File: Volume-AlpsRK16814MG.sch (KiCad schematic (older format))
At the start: 9 parts, among them P1 AB I/O, P2 CD I/O, P3 VD, P4 CTRL, P5 GND, U1 SN754410

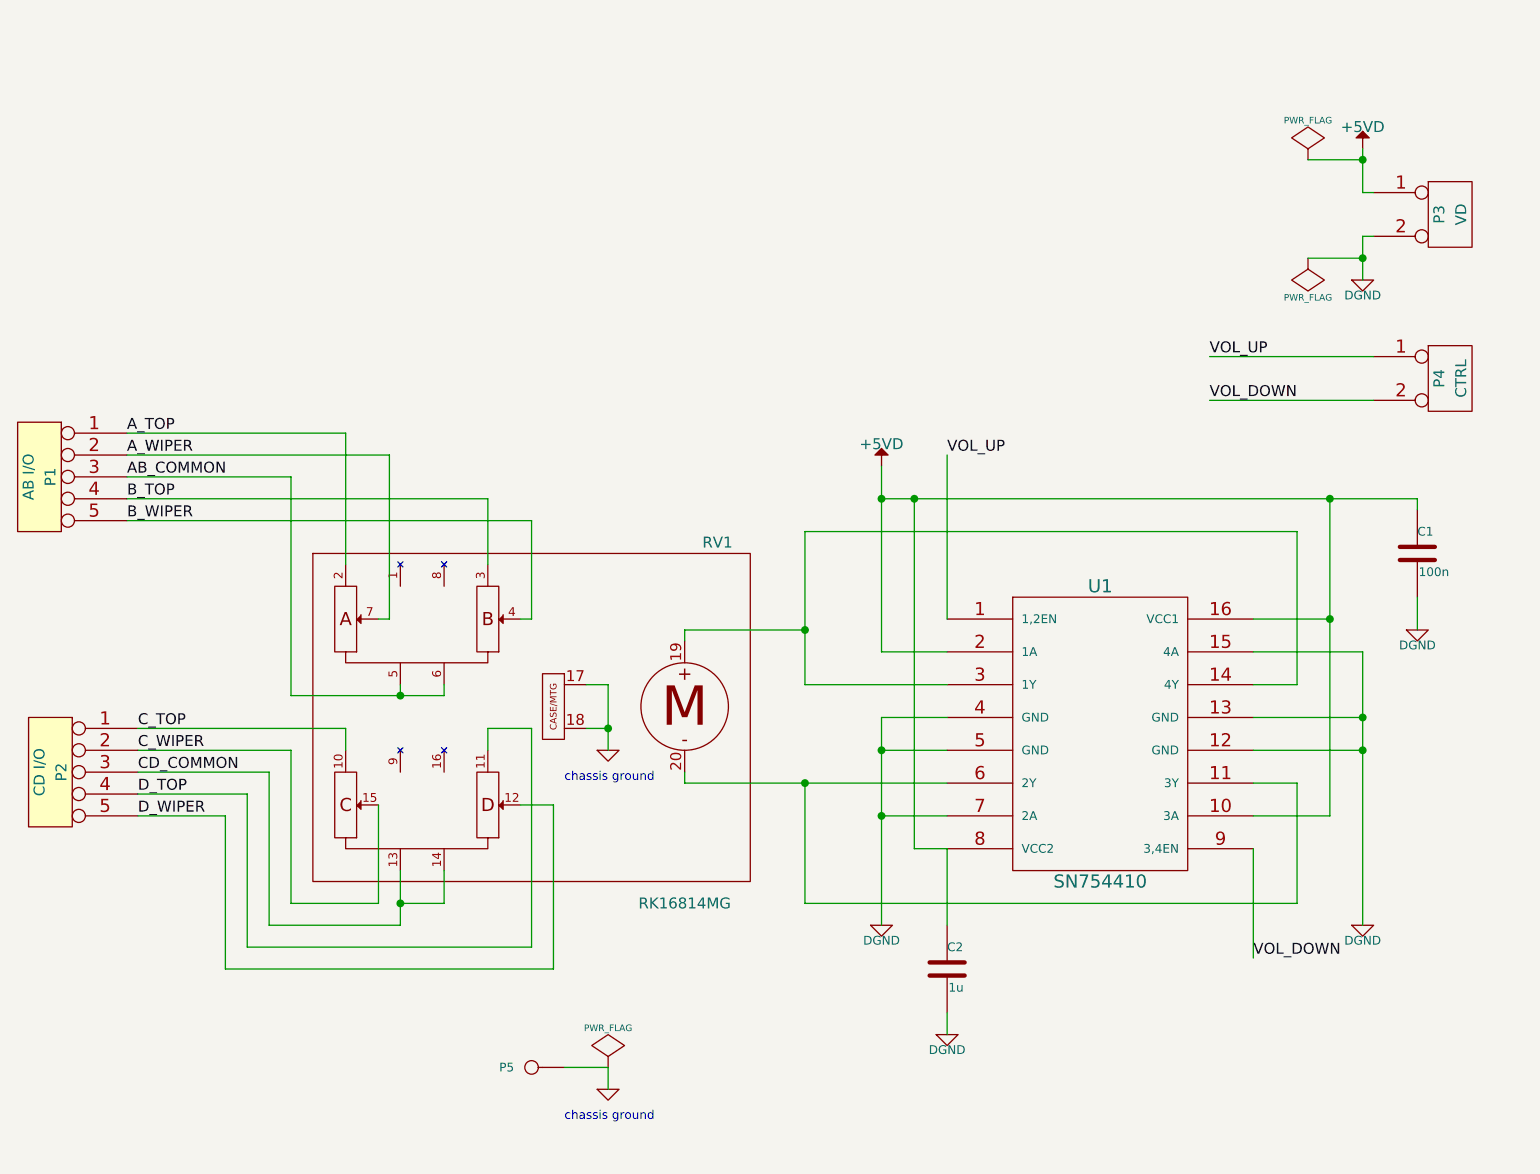
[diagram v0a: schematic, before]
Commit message: Silkscreen optimizations. Added license to silkscreen.
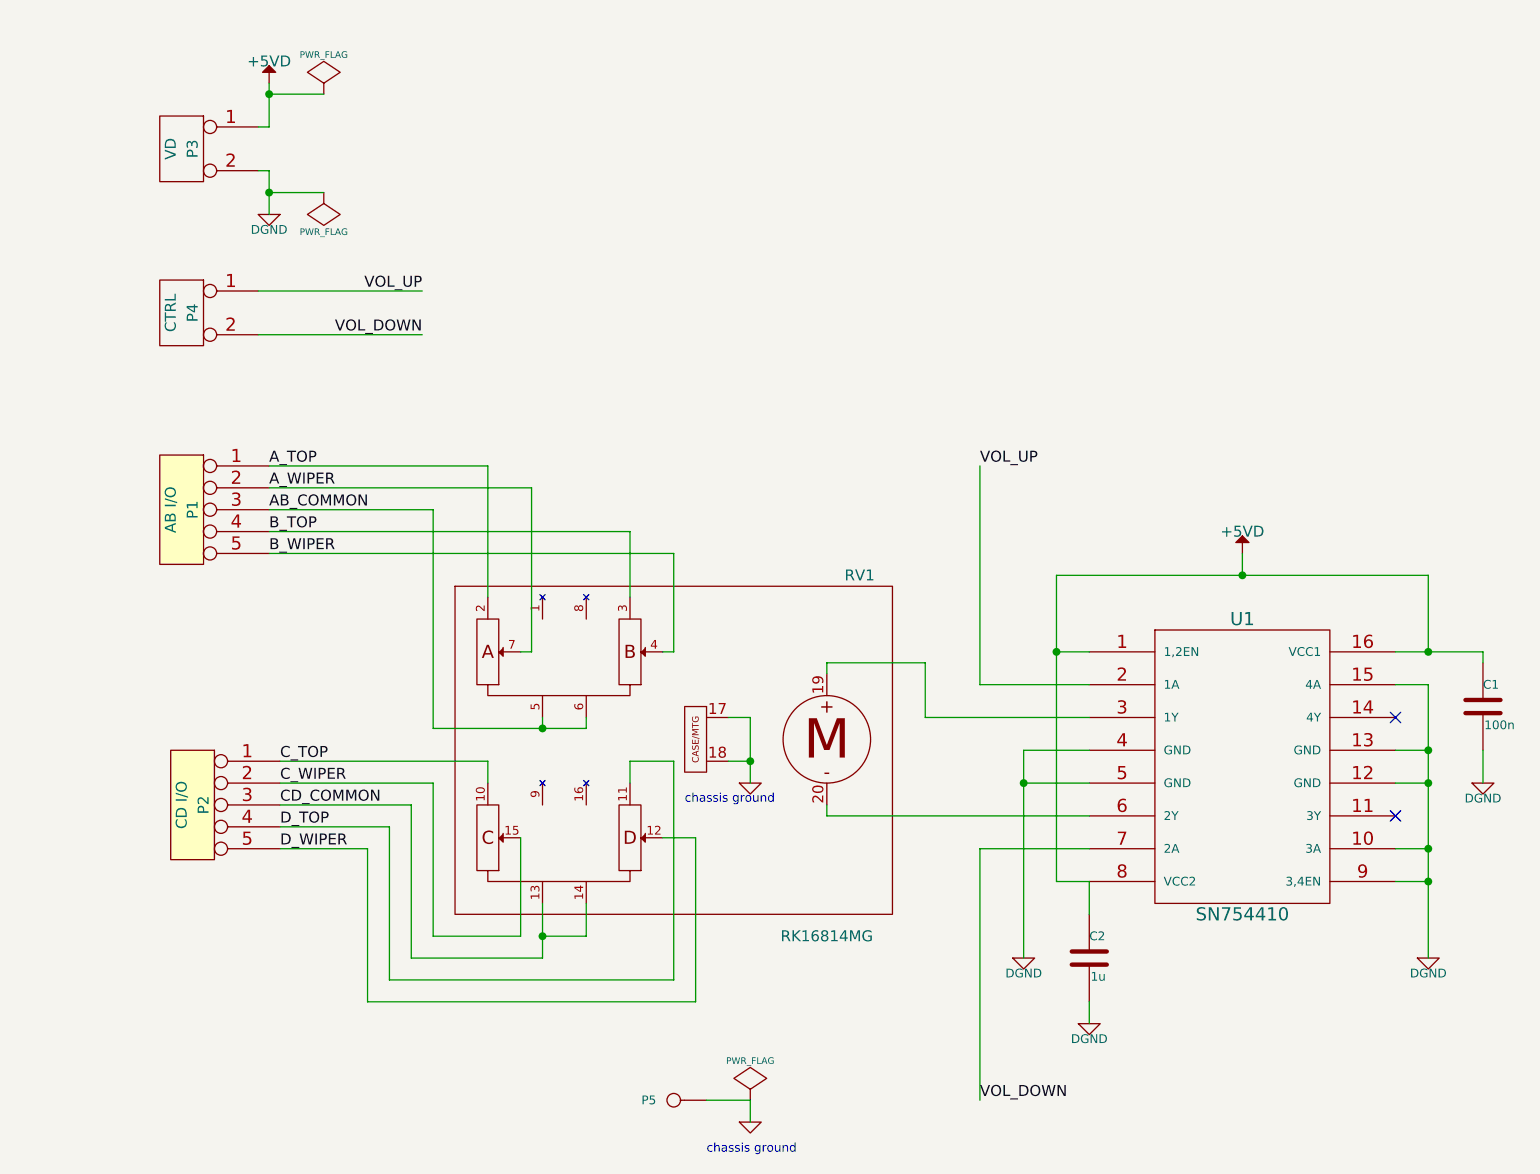
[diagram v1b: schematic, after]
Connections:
- net +5VD: now also U1.1 (1,2EN); no longer U1.10 (3A), U1.2 (1A)
- net DGND: now also U1.10 (3A), U1.9 (3,4EN); no longer U1.7 (2A)
- net VOL_DOWN: now also U1.7 (2A); no longer U1.9 (3,4EN)
- net VOL_UP: now also U1.2 (1A); no longer U1.1 (1,2EN)
- net at RV1.20 (Vmotor-), U1.6 (2Y): no longer U1.11 (3Y)
- net at RV1.19 (Vmotor+), U1.3 (1Y): no longer U1.14 (4Y)
- no-connect marks 0 -> 2
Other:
- moved on the sheet: C1, C2, P1, P2, P3, P4, P5, RV1, U1

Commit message: Schematic changes for independent motor drive voltage.
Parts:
- removed P3: VD, mfk-TE_282834-2, symbol CONN_2
- added P3: V, symbol CONN_3
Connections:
- net +5VD: now also P3.2 (PM); no longer C2.1, U1.8 (VCC2)
- net DGND: now also P3.3 (P3)
- new net V_MOTOR: C2.1, P3.1 (P1), U1.8 (VCC2)
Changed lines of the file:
@@
 Sheet 1 1
 Title "ALPS RK16816MG with H-bridge"
-Date "24 mar 2015"
+Date "3 apr 2015"
 Rev ""
 Comp "Mithat Konar"
@@
 L DGND #PWR02
 U 1 1 550CA86E
-P 6600 5500
-F 0 "#PWR02" H 6600 5500 40  0001 C CNN
-F 1 "DGND" H 6600 5430 40  0000 C CNN
-F 2 "" H 6600 5500 60  0000 C CNN
-F 3 "" H 6600 5500 60  0000 C CNN
-	1    6600 5500
+P 6600 5300
+F 0 "#PWR02" H 6600 5300 40  0001 C CNN
+F 1 "DGND" H 6600 5230 40  0000 C CNN
+F 2 "" H 6600 5300 60  0000 C CNN
+F 3 "" H 6600 5300 60  0000 C CNN
+	1    6600 5300
 	1    0    0    -1
 $EndComp
@@
 	6900 4550 6600 4550
 Wire Wire Line
-	6600 4550 6600 5500
+	6600 4550 6600 5300
 Wire Wire Line
 	6900 4700 6600 4700
@@
 Wire Wire Line
 	6750 5150 6900 5150
-Wire Wire Line
-	6750 3750 6750 5150
 $Comp
 L C C1
@@
 Wire Wire Line
 	8700 4700 8700 4550
-Text Label 6400 3250 0    50   ~ 0
+Text Label 6400 3250 3    50   ~ 0
 VOL_UP
-Text Label 6400 6150 0    50   ~ 0
+Text Label 6400 6150 1    50   ~ 0
 VOL_DOWN
 $Comp
@@
 $EndComp
 Wire Wire Line
-	3150 1700 3100 1700
-Wire Wire Line
-	3150 1500 3150 1700
+	3650 1350 3650 1800
 Wire Wire Line
 	3100 2450 3850 2450
@@
 L PWR_FLAG #FLG06
 U 1 1 550CB3CC
-P 3400 1550
-F 0 "#FLG06" H 3400 1645 30  0001 C CNN
-F 1 "PWR_FLAG" H 3400 1730 30  0000 C CNN
-F 2 "" H 3400 1550 60  0000 C CNN
-F 3 "" H 3400 1550 60  0000 C CNN
-	1    3400 1550
+P 3900 1650
+F 0 "#FLG06" H 3900 1745 30  0001 C CNN
+F 1 "PWR_FLAG" H 3900 1830 30  0000 C CNN
+F 2 "" H 3900 1650 60  0000 C CNN
+F 3 "" H 3900 1650 60  0000 C CNN
+	1    3900 1650
 	-1   0    0    -1
 $EndComp
@@
 	3150 1900 3150 2100
 Wire Wire Line
-	3400 1550 3150 1550
-Connection ~ 3150 1550
+	3900 1650 3650 1650
+Connection ~ 3650 1650
 Wire Wire Line
 	3400 2000 3150 2000
 Connection ~ 3150 2000
-$Comp
-L CONN_2 P3
-U 1 1 550CCC99
-P 2750 1800
-F 0 "P3" V 2700 1800 50  0000 C CNN
-F 1 "VD" V 2800 1800 50  0000 C CNN
-F 2 "mfk-TE_282834-2" H 2750 1800 60  0001 C CNN
-F 3 "" H 2750 1800 60  0000 C CNN
-	1    2750 1800
-	-1   0    0    -1
-$EndComp
 $Comp
 L CONN_2 P4
@@
 L +5VD #PWR08
 U 1 1 550CE733
-P 3150 1500
-F 0 "#PWR08" H 3150 1450 20  0001 C CNN
-F 1 "+5VD" H 3150 1600 50  0000 C CNN
-F 2 "" H 3150 1500 60  0000 C CNN
-F 3 "" H 3150 1500 60  0000 C CNN
-	1    3150 1500
+P 3650 1350
+F 0 "#PWR08" H 3650 1300 20  0001 C CNN
+F 1 "+5VD" H 3650 1450 50  0000 C CNN
+F 2 "" H 3650 1350 60  0000 C CNN
+F 3 "" H 3650 1350 60  0000 C CNN
+	1    3650 1350
 	-1   0    0    -1
 $EndComp
@@
 63 98 05 E1 6B C4 72 91 8E EA 95 27 8C 4B 0B 6B 30 6B 95 2D 08 DF 47 79 14 D8 40 20 A9 90 96 2D
 E1 E7 3D C6 74 F3 E0 6E B9 00 E4 0E CC EC 2A 00 9E 03 F9 2E 43 53 93 3B E7 B1 3D FE 0F E4 2C B5
-B8 3A B8 3B 5D 00 00 00 00 49 45 4E 44 AE 42 60 82 30 $EndBitmap
+B8 3A B8 3B 5D 00 00 00 00 49 45 4E 44 AE 42 60 82 69 $EndBitmap
 EndData
 $EndBitmap
@@
 Wire Wire Line
 	6900 4100 6750 4100
-Connection ~ 6750 4100
 Wire Wire Line
 	6150 4150 6150 4400
@@
 Wire Wire Line
 	6400 5000 6400 6150
+$Comp
+L CONN_3 P3
+U 1 1 551F2247
+P 2750 1800
+F 0 "P3" V 2700 1800 50  0000 C CNN
+F 1 "V" V 2800 1800 40  0000 C CNN
+F 2 "" H 2750 1800 60  0000 C CNN
+F 3 "" H 2750 1800 60  0000 C CNN
+	1    2750 1800
+	-1   0    0    -1
+$EndComp
+Wire Wire Line
+	3650 1800 3100 1800
+Wire Wire Line
+	3100 1700 3350 1700
+Wire Wire Line
+	3150 1250 3150 1700
+Text Label 3150 1250 3    60   ~ 0
+V_MOTOR
+Wire Wire Line
+	6750 4100 6750 3750
+Wire Wire Line
+	6750 5150 6750 6150
+Text Label 6750 6150 1    60   ~ 0
+V_MOTOR
+$Comp
+L PWR_FLAG #FLG013
+U 1 1 551F243F
+P 3350 1650
+F 0 "#FLG013" H 3350 1745 30  0001 C CNN
+F 1 "PWR_FLAG" H 3350 1830 30  0000 C CNN
+F 2 "" H 3350 1650 60  0000 C CNN
+F 3 "" H 3350 1650 60  0000 C CNN
+	1    3350 1650
+	-1   0    0    -1
+$EndComp
+Connection ~ 3150 1700
+Wire Wire Line
+	3350 1700 3350 1650
 $EndSCHEMATC

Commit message: Added jumper to connect motor and digital supplies to schematic; PCB updated.
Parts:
- added J1: PWR_BR, mfk-SIL-2, symbol JUMPER
- P3: value V -> PWR; footprint (none) -> mfk-TE_282834-3
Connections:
- net +5VD: now also J1.1
- net V_MOTOR renamed V_MOT
- net V_MOT: now also J1.2
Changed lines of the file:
@@
 Sheet 1 1
 Title "ALPS RK16816MG with H-bridge"
-Date "3 apr 2015"
+Date "4 apr 2015"
 Rev ""
 Comp "Mithat Konar"
@@
 63 98 05 E1 6B C4 72 91 8E EA 95 27 8C 4B 0B 6B 30 6B 95 2D 08 DF 47 79 14 D8 40 20 A9 90 96 2D
 E1 E7 3D C6 74 F3 E0 6E B9 00 E4 0E CC EC 2A 00 9E 03 F9 2E 43 53 93 3B E7 B1 3D FE 0F E4 2C B5
-B8 3A B8 3B 5D 00 00 00 00 49 45 4E 44 AE 42 60 82 69 $EndBitmap
+B8 3A B8 3B 5D 00 00 00 00 49 45 4E 44 AE 42 60 82 14 $EndBitmap
 EndData
 $EndBitmap
@@
 P 2750 1800
 F 0 "P3" V 2700 1800 50  0000 C CNN
-F 1 "V" V 2800 1800 40  0000 C CNN
-F 2 "" H 2750 1800 60  0000 C CNN
+F 1 "PWR" V 2800 1800 40  0000 C CNN
+F 2 "mfk-TE_282834-3" H 2750 1800 60  0001 C CNN
 F 3 "" H 2750 1800 60  0000 C CNN
 	1    2750 1800
@@
 	3150 1250 3150 1700
 Text Label 3150 1250 3    60   ~ 0
-V_MOTOR
+V_MOT
 Wire Wire Line
 	6750 4100 6750 3750
@@
 	6750 5150 6750 6150
 Text Label 6750 6150 1    60   ~ 0
-V_MOTOR
+V_MOT
 $Comp
 L PWR_FLAG #FLG013
@@
 Wire Wire Line
 	3350 1700 3350 1650
+$Comp
+L JUMPER J1
+U 1 1 552023B1
+P 4750 1800
+F 0 "J1" H 4750 1950 60  0000 C CNN
+F 1 "PWR_BR" H 4750 1720 40  0000 C CNN
+F 2 "mfk-SIL-2" H 4750 1800 60  0001 C CNN
+F 3 "~" H 4750 1800 60  0000 C CNN
+	1    4750 1800
+	1    0    0    -1
+$EndComp
+$Comp
+L +5VD #PWR014
+U 1 1 552023F3
+P 4400 1450
+F 0 "#PWR014" H 4400 1400 20  0001 C CNN
+F 1 "+5VD" H 4400 1550 50  0000 C CNN
+F 2 "" H 4400 1450 60  0000 C CNN
+F 3 "" H 4400 1450 60  0000 C CNN
+	1    4400 1450
+	-1   0    0    -1
+$EndComp
+Wire Wire Line
+	4450 1800 4400 1800
+Wire Wire Line
+	4400 1800 4400 1450
+Text Label 5100 1350 3    60   ~ 0
+V_MOT
+Wire Wire Line
+	5050 1800 5100 1800
+Wire Wire Line
+	5100 1800 5100 1350
 $EndSCHEMATC

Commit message: .gitignore ignores top-level zip, png, and svg files. Added docs dir.
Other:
- note added: "Use jumper to power motor from +5VD."
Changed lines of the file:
@@
 63 98 05 E1 6B C4 72 91 8E EA 95 27 8C 4B 0B 6B 30 6B 95 2D 08 DF 47 79 14 D8 40 20 A9 90 96 2D
 E1 E7 3D C6 74 F3 E0 6E B9 00 E4 0E CC EC 2A 00 9E 03 F9 2E 43 53 93 3B E7 B1 3D FE 0F E4 2C B5
-B8 3A B8 3B 5D 00 00 00 00 49 45 4E 44 AE 42 60 82 14 $EndBitmap
+B8 3A B8 3B 5D 00 00 00 00 49 45 4E 44 AE 42 60 82 AC $EndBitmap
 EndData
 $EndBitmap
@@
 Wire Wire Line
 	5100 1800 5100 1350
+Text Notes 4000 2000 0    60   ~ 0
+Use jumper to power motor from +5VD.
 $EndSCHEMATC

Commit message: Changed labels on PCB and schematic so names are consistent. Readme tweak.
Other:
- note added: "CHASSIS GND"
- note removed: "chassis ground"
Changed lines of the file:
@@
 Sheet 1 1
 Title "ALPS RK16816MG with H-bridge"
-Date "4 apr 2015"
+Date "9 apr 2015"
 Rev ""
 Comp "Mithat Konar"
@@
 63 98 05 E1 6B C4 72 91 8E EA 95 27 8C 4B 0B 6B 30 6B 95 2D 08 DF 47 79 14 D8 40 20 A9 90 96 2D
 E1 E7 3D C6 74 F3 E0 6E B9 00 E4 0E CC EC 2A 00 9E 03 F9 2E 43 53 93 3B E7 B1 3D FE 0F E4 2C B5
-B8 3A B8 3B 5D 00 00 00 00 49 45 4E 44 AE 42 60 82 AC $EndBitmap
+B8 3A B8 3B 5D 00 00 00 00 49 45 4E 44 AE 42 60 82 33 $EndBitmap
 EndData
 $EndBitmap
@@
 	5350 4400 5350 4700
 Connection ~ 5350 4600
-Text Notes 5050 4800 0    40   ~ 0
-chassis ground
+Text Notes 5150 4850 0    40   ~ 0
+CHASSIS GND
 $Comp
 L GND #PWR010
@@
 $EndComp
 Text Notes 5150 6400 0    40   ~ 0
-chassis ground
+CHASSIS GND
 $Comp
 L PWR_FLAG #FLG011
